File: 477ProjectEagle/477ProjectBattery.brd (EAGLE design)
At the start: 100 x 80 mm, 21 parts

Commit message: Worked on Battery PCB
Finished up the Battery PCB
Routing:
- net GNDA: track 136.9 -> 50.3 mm
- net +3V3: track 135.7 -> 85.6 mm
- net N$36: track 45.8 -> 0.00 mm
- net N$4: track 76.7 -> 56.7 mm
- net N$6: track 22.5 -> 23.1 mm
- net N$5: track 21.5 -> 22.0 mm
- added copper zone on layer 1, net GND
- added copper zone on layer 16, net GNDA
- added copper zone on layer 1, net N$3

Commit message: Battery PCB
finished up board
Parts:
- moved U$7 1.22 mm to (39.2, 49.6)
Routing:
- net N$4: track 56.7 -> 33.2 mm, vias 2 -> 0
- net GNDA: track 50.3 -> 47.7 mm, vias 2 -> 1
- added copper zone on layer 1, net N$2

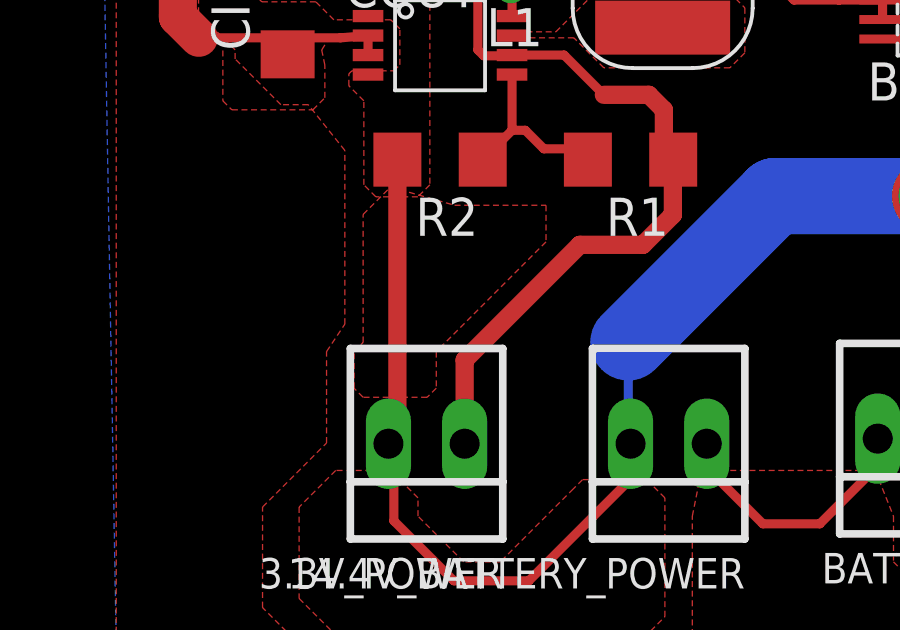
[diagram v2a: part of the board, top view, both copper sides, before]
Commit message: Did a lot of work on the PCB design
Added headers to pad out all micro pins. Routed pretty much everything
to where it needs to go. Just need to fix hbridge and check accuracy of
connections
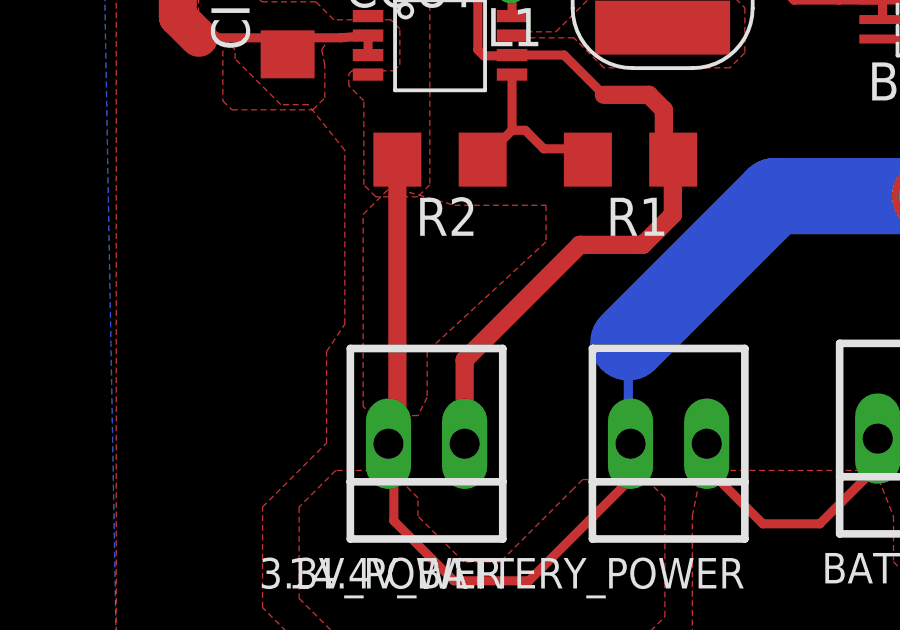
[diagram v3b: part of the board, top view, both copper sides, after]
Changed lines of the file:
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@@
 <setting verticaltext="up"/>
 </settings>
-<grid distance="0.05" unitdist="inch" unit="inch" style="lines" multiple="1" display="yes" altdistance="0.005" altunitdist="inch" altunit="inch"/>
+<grid distance="1" unitdist="inch" unit="inch" style="lines" multiple="1" display="yes" altdistance="0.005" altunitdist="inch" altunit="inch"/>
 <layers>
 <layer number="1" name="Top" color="4" fill="1" visible="yes" active="yes"/>
@@
 <vertex x="42.672" y="32.9184"/>
 <vertex x="42.672" y="31.6992"/>
-<vertex x="39.0144" y="28.0416"/>
-<vertex x="39.0144" y="26.8224"/>
+<vertex x="38.7096" y="28.0416"/>
 <vertex x="38.7096" y="26.5176"/>
-<vertex x="36.576" y="26.5176"/>
-<vertex x="36.2712" y="26.8224"/>
-<vertex x="36.2712" y="28.0416"/>
-<vertex x="36.576" y="28.3464"/>
+<vertex x="38.4048" y="25.908"/>
+<vertex x="36.8808" y="25.908"/>
+<vertex x="36.576" y="26.2128"/>
 </polygon>
 <wire x1="37.6" y1="25.9" x2="37.42" y2="24.97" width="0" layer="19" extent="1-1"/>

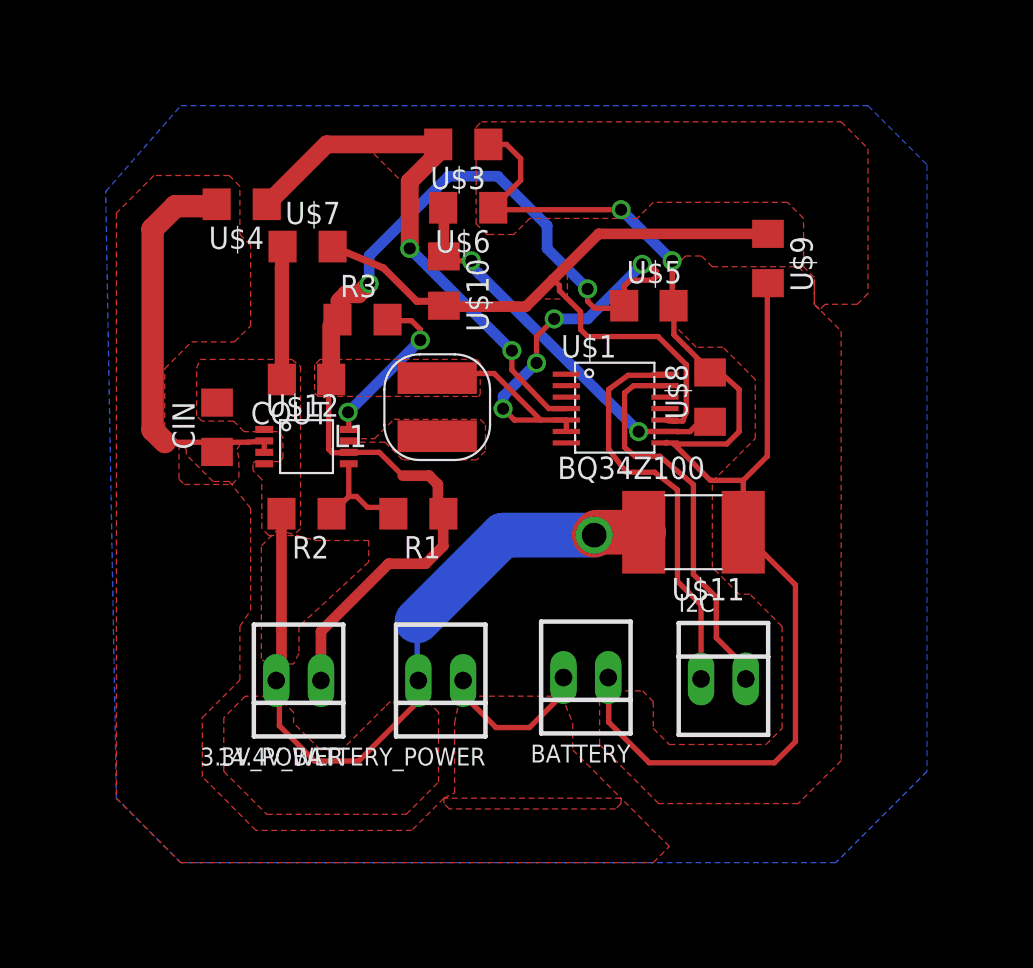
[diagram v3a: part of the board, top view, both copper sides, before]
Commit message: Battery PCB
Finished up battery pcb, got rid of acute angles and turned off
thermals.
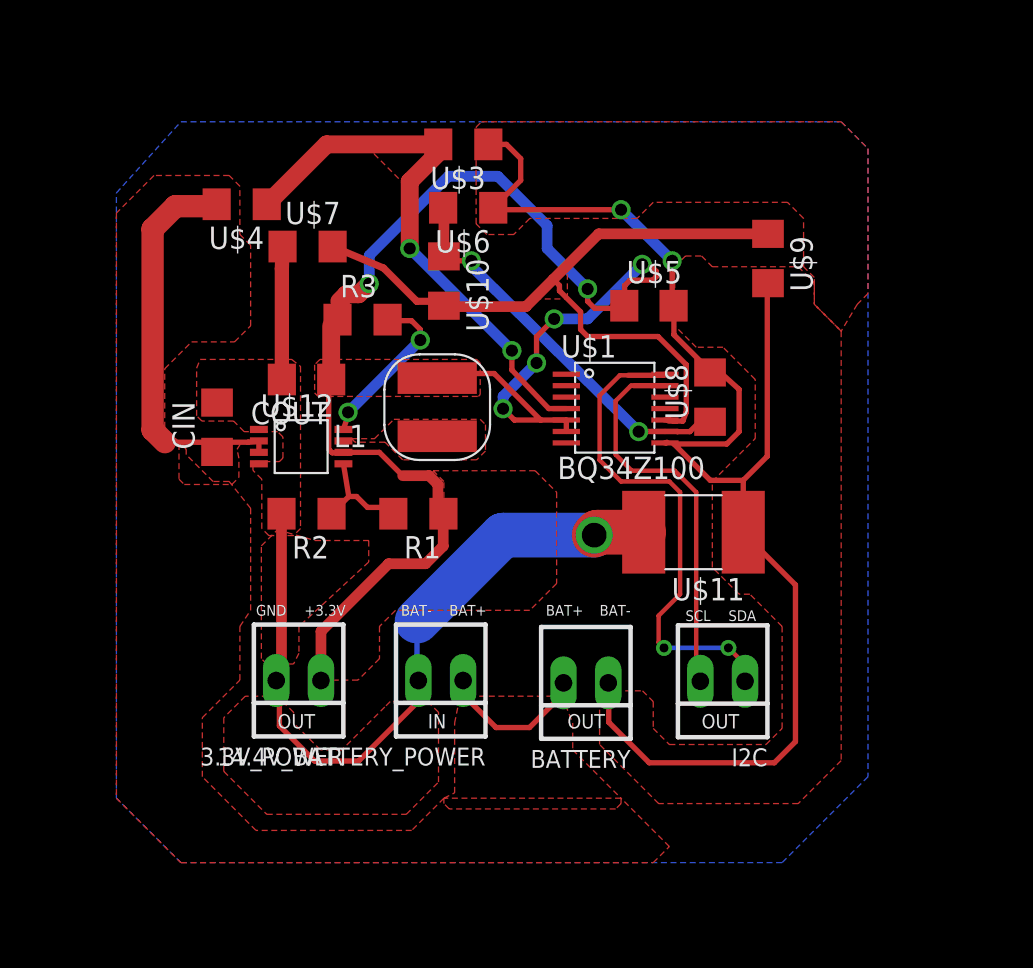
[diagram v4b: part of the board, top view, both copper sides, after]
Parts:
- moved BATTERY 0.30 mm to (55.0, 24.8)
- moved U$12 0.30 mm to (38.8, 38.2)
- moved I2C 0.14 mm to (62.8, 24.9), turned to 180 degrees
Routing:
- net N$6: track 23.1 -> 28.6 mm, vias 0 -> 2
- net +3V3: track 85.6 -> 86.2 mm
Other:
- board text added: "+3.3V"
- board text added: "BAT+"
- board text added: "BAT-"
- board text added: "GND"
- board text added: "IN"
- board text added: "OUT"
- board text added: "SCL"
- board text added: "SDA"

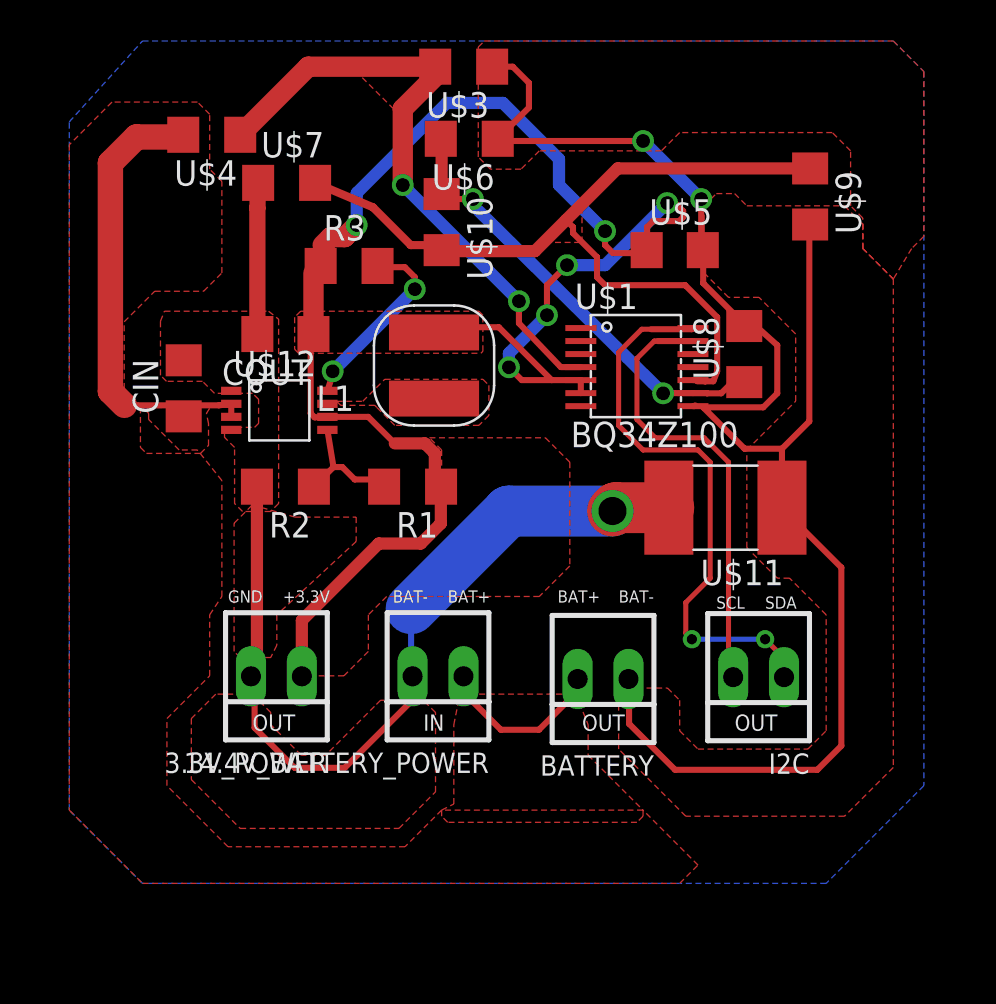
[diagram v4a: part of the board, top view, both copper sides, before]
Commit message: Fixed the silkscreen display w/ batt board
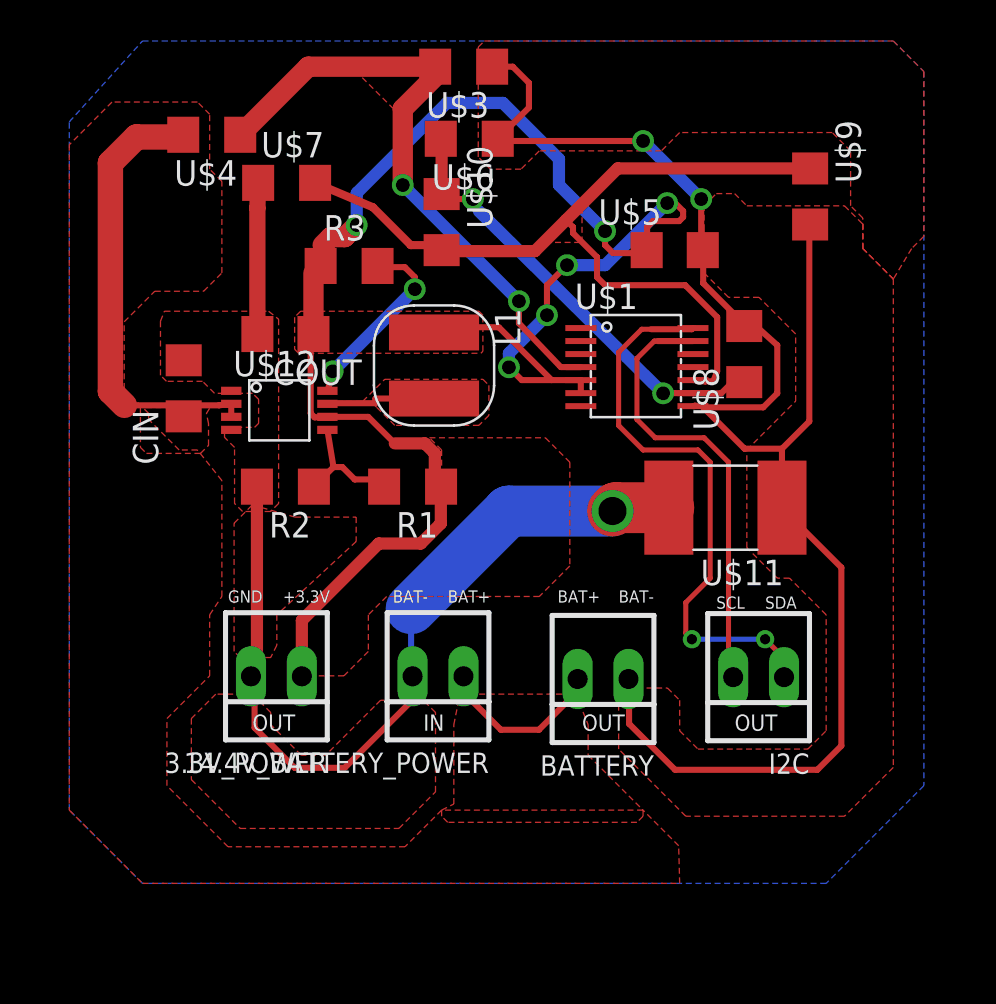
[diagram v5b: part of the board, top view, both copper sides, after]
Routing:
- net N$36: track 0.00 -> 5.59 mm
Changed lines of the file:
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@@
 <setting verticaltext="up"/>
 </settings>
-<grid distance="12" unitdist="mil" unit="mil" style="lines" multiple="1" display="yes" altdistance="0.005" altunitdist="inch" altunit="inch"/>
+<grid distance="2" unitdist="mil" unit="mil" style="lines" multiple="1" display="yes" altdistance="0.005" altunitdist="inch" altunit="inch"/>
 <layers>
 <layer number="1" name="Top" color="4" fill="1" visible="yes" active="yes"/>
@@
 <layer number="23" name="tOrigins" color="15" fill="1" visible="yes" active="yes"/>
 <layer number="24" name="bOrigins" color="15" fill="1" visible="yes" active="yes"/>
-<layer number="25" name="tNames" color="7" fill="1" visible="no" active="yes"/>
+<layer number="25" name="tNames" color="7" fill="1" visible="yes" active="yes"/>
 <layer number="26" name="bNames" color="7" fill="1" visible="no" active="yes"/>
-<layer number="27" name="tValues" color="7" fill="1" visible="no" active="yes"/>
+<layer number="27" name="tValues" color="7" fill="1" visible="yes" active="yes"/>
 <layer number="28" name="bValues" color="7" fill="1" visible="no" active="yes"/>
 <layer number="29" name="tStop" color="7" fill="3" visible="no" active="yes"/>
@@
 <vertex x="41.8" y="38.6"/>
 </polygon>
+<wire x1="46.56" y1="38.84" x2="43.6372" y2="38.84" width="0.3048" layer="1"/>
+<wire x1="43.6372" y1="38.84" x2="43.6372" y2="38.608" width="0.3048" layer="1"/>
+<wire x1="43.6372" y1="38.608" x2="41.2352" y2="38.608" width="0.3048" layer="1"/>
+<wire x1="41.2352" y1="38.608" x2="41.2352" y2="38.575" width="0.3048" layer="1"/>
 </signal>
 <signal name="N$37">
@@
 <vertex x="32.004" y="14.6304"/>
 <vertex x="58.8264" y="14.6304"/>
-<vertex x="59.7408" y="15.5448"/>
-</polygon>
-</signal>
+<vertex x="58.7756" y="16.51"/>
+</polygon>
+</signal>
